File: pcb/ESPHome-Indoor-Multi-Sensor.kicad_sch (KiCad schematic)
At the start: 11 parts, among them J2 USB-C, U9 INA228

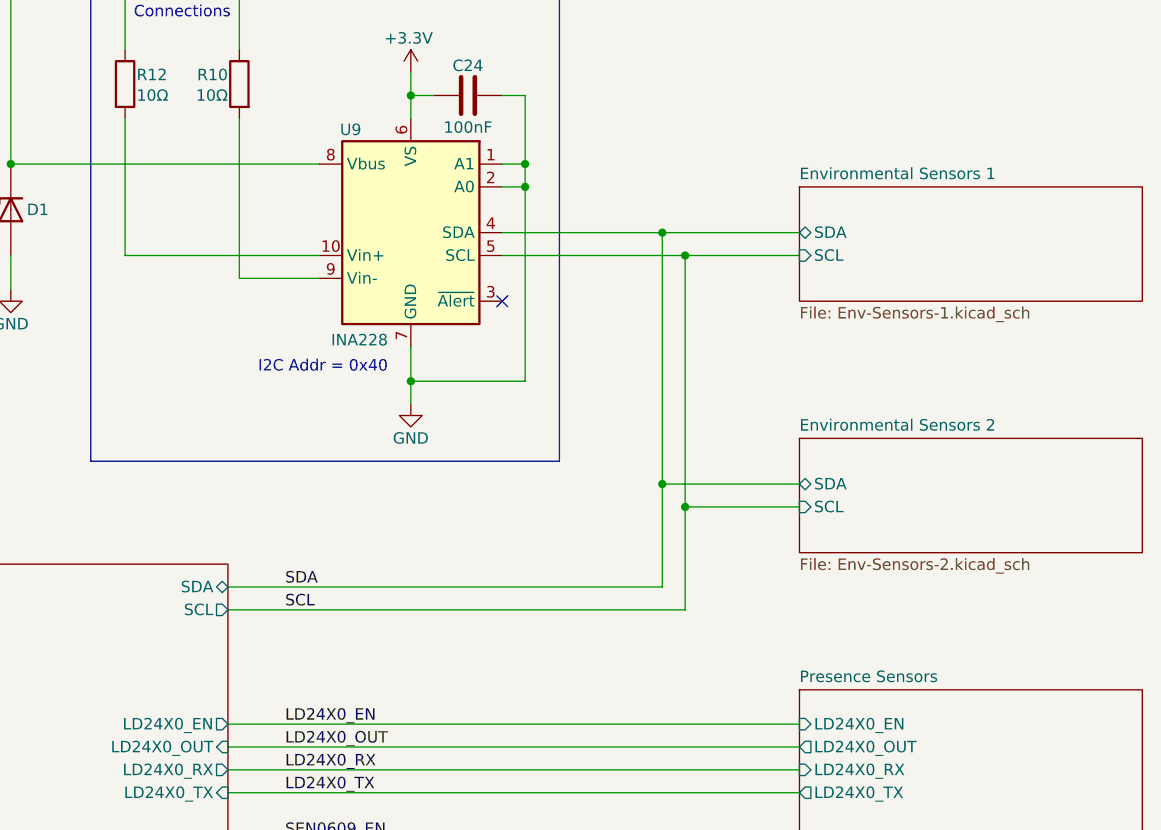
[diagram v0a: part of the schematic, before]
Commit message: Minor changes
Separate SEN66 on a separate I2C bus.
Add WIFi Antenna cutout.
Beef-up Power and Ground connections to SEN66.
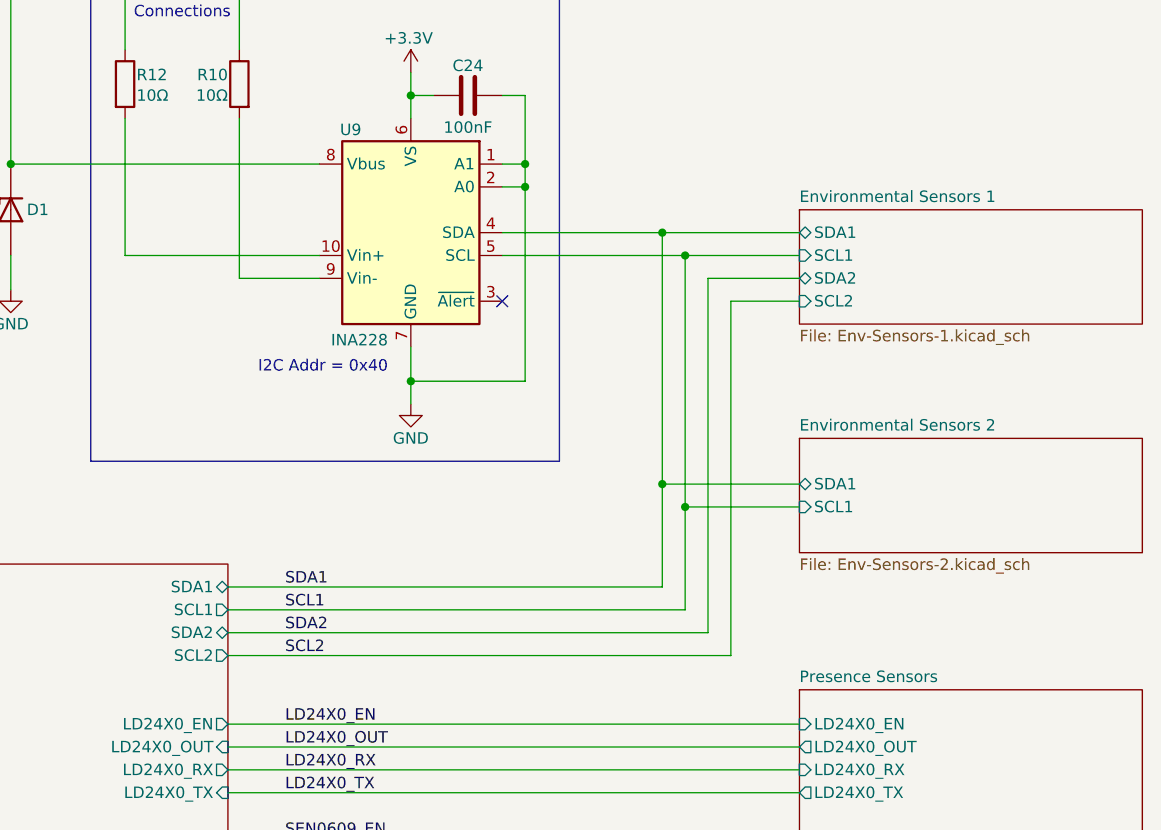
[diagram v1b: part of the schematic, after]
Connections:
- net SCL renamed SCL1
- net SDA renamed SDA1
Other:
- sheet ESP32-S3 ports: added SCL1, SCL2, SDA1, SDA2; removed SCL, SDA
- sheet Environmental Sensors 1 ports: added SCL1, SCL2, SDA1, SDA2; removed SCL, SDA
- sheet Environmental Sensors 2 ports: added SCL1, SDA1; removed SCL, SDA
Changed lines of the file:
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@@
 	(title_block
 		(title "ESPHome Parking Assistant")
-		(date "2025-04-10")
-		(rev "-")
+		(date "2025-04-18")
+		(rev "A")
 		(company "Mike Lawrence")
 	)
@@
 	(wire
 		(pts
+			(xy 203.2 83.82) (xy 195.58 83.82)
+		)
+		(stroke
+			(width 0)
+			(type default)
+		)
+	)
+	(wire
+		(pts
 			(xy 73.66 44.45) (xy 76.2 44.45)
 		)
@@
 	(wire
 		(pts
+			(xy 203.2 81.28) (xy 193.04 81.28)
+		)
+		(stroke
+			(width 0)
+			(type default)
+		)
+	)
+	(wire
+		(pts
 			(xy 115.57 31.75) (xy 128.27 31.75)
 		)
@@
 	(wire
 		(pts
+			(xy 193.04 81.28) (xy 193.04 120.65)
+		)
+		(stroke
+			(width 0)
+			(type default)
+		)
+	)
+	(wire
+		(pts
 			(xy 140.97 55.88) (xy 140.97 31.75)
 		)
@@
 	(wire
 		(pts
+			(xy 139.7 120.65) (xy 193.04 120.65)
+		)
+		(stroke
+			(width 0)
+			(type default)
+		)
+	)
+	(wire
+		(pts
 			(xy 90.17 44.45) (xy 90.17 119.38)
 		)
@@
 	(wire
 		(pts
+			(xy 139.7 123.19) (xy 195.58 123.19)
+		)
+		(stroke
+			(width 0)
+			(type default)
+		)
+	)
+	(wire
+		(pts
 			(xy 128.27 78.74) (xy 128.27 63.5)
 		)
@@
 	(wire
 		(pts
+			(xy 195.58 83.82) (xy 195.58 123.19)
+		)
+		(stroke
+			(width 0)
+			(type default)
+		)
+	)
+	(wire
+		(pts
 			(xy 93.98 77.47) (xy 93.98 82.55)
 		)
@@
 				)
 			)
-			(table_cell "0x68"
+			(table_cell "0x6B"
 				(exclude_from_sim no)
 				(at 228.6 46.99 0)
@@
 		)
 	)
+	(label "SDA2"
+		(at 146.05 120.65 0)
+		(effects
+			(font
+				(size 1.27 1.27)
+			)
+			(justify left bottom)
+		)
+	)
 	(label "LD24X0_OUT"
 		(at 146.05 133.35 0)
@@
 		)
 	)
-	(label "SCL"
+	(label "SCL1"
 		(at 146.05 118.11 0)
 		(effects
@@
 		)
 	)
-	(label "SDA"
+	(label "SDA1"
 		(at 146.05 115.57 0)
 		(effects
@@
 		)
 	)
+	(label "SCL2"
+		(at 146.05 123.19 0)
+		(effects
+			(font
+				(size 1.27 1.27)
+			)
+			(justify left bottom)
+		)
+	)
 	(label "LD24X0_RX"
 		(at 146.05 135.89 0)
@@
 			)
 		)
-		(pin "SCL" input
+		(pin "SCL1" input
 			(at 203.2 106.68 180)
 			(effects
@@
 			)
 		)
-		(pin "SDA" bidirectional
+		(pin "SDA1" bidirectional
 			(at 203.2 104.14 180)
 			(effects
@@
 			)
 		)
-		(pin "SDA" bidirectional
+		(pin "SDA1" bidirectional
 			(at 139.7 115.57 0)
 			(effects
@@
 			)
 		)
-		(pin "SCL" output
+		(pin "SCL1" output
 			(at 139.7 118.11 0)
 			(effects
@@
 			)
 		)
+		(pin "SCL2" output
+			(at 139.7 123.19 0)
+			(effects
+				(font
+					(size 1.27 1.27)
+				)
+				(justify right)
+			)
+		)
+		(pin "SDA2" bidirectional
+			(at 139.7 120.65 0)
+			(effects
+				(font
+					(size 1.27 1.27)
+				)
+				(justify right)
+			)
+		)
 		(instances
 			(project "ESPHome-Indoor-Multi-Sensor"
@@
 	)
 	(sheet
-		(at 203.2 71.12)
+		(at 203.2 73.66)
 		(size 38.1 12.7)
 		(exclude_from_sim no)
@@
 		)
 		(property "Sheetname" "Environmental Sensors 1"
-			(at 203.2 70.4084 0)
+			(at 203.2 72.9484 0)
 			(effects
 				(font
@@
 		)
 		(property "Sheetfile" "Env-Sensors-1.kicad_sch"
-			(at 203.2 84.4046 0)
+			(at 203.2 86.9446 0)
 			(effects
 				(font
@@
 			)
 		)
-		(pin "SCL" input
+		(pin "SCL1" input
 			(at 203.2 78.74 180)
 			(effects
@@
 			)
 		)
-		(pin "SDA" bidirectional
+		(pin "SDA1" bidirectional
 			(at 203.2 76.2 180)
 			(effects
 				(font
+					(size 1.27 1.27)
+				)
+				(justify left)
+			)
+		)
+		(pin "SCL2" input
+			(at 203.2 83.82 180)
+			(effects
+				(font
+					(size 1.27 1.27)
+				)
+				(justify left)
+			)
+		)
+		(pin "SDA2" bidirectional
+			(at 203.2 81.28 180)
+			(effects
+				(font
